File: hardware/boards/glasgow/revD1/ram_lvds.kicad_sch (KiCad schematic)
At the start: 37 parts, among them J11 CLK_EXT, J12 FPGA_TP, J6 LVDS, U11 XccelaOPI, U12 XccelaOPI, U8 LFE5U-25F-8BG256x, Y3 Si5351A-B-GM1, Y4 25M

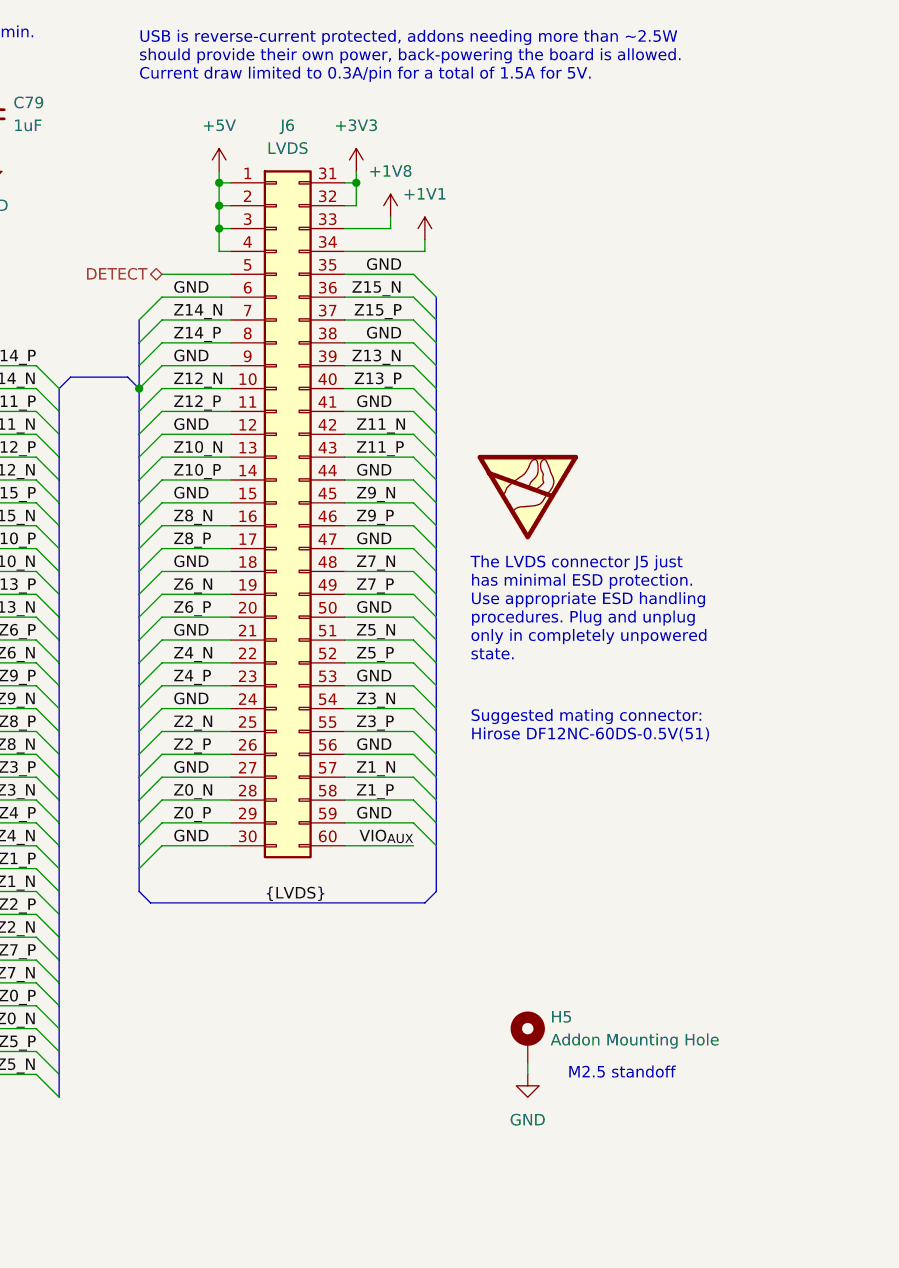
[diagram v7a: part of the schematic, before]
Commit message: update LVDS connector
add more ground test points on the back
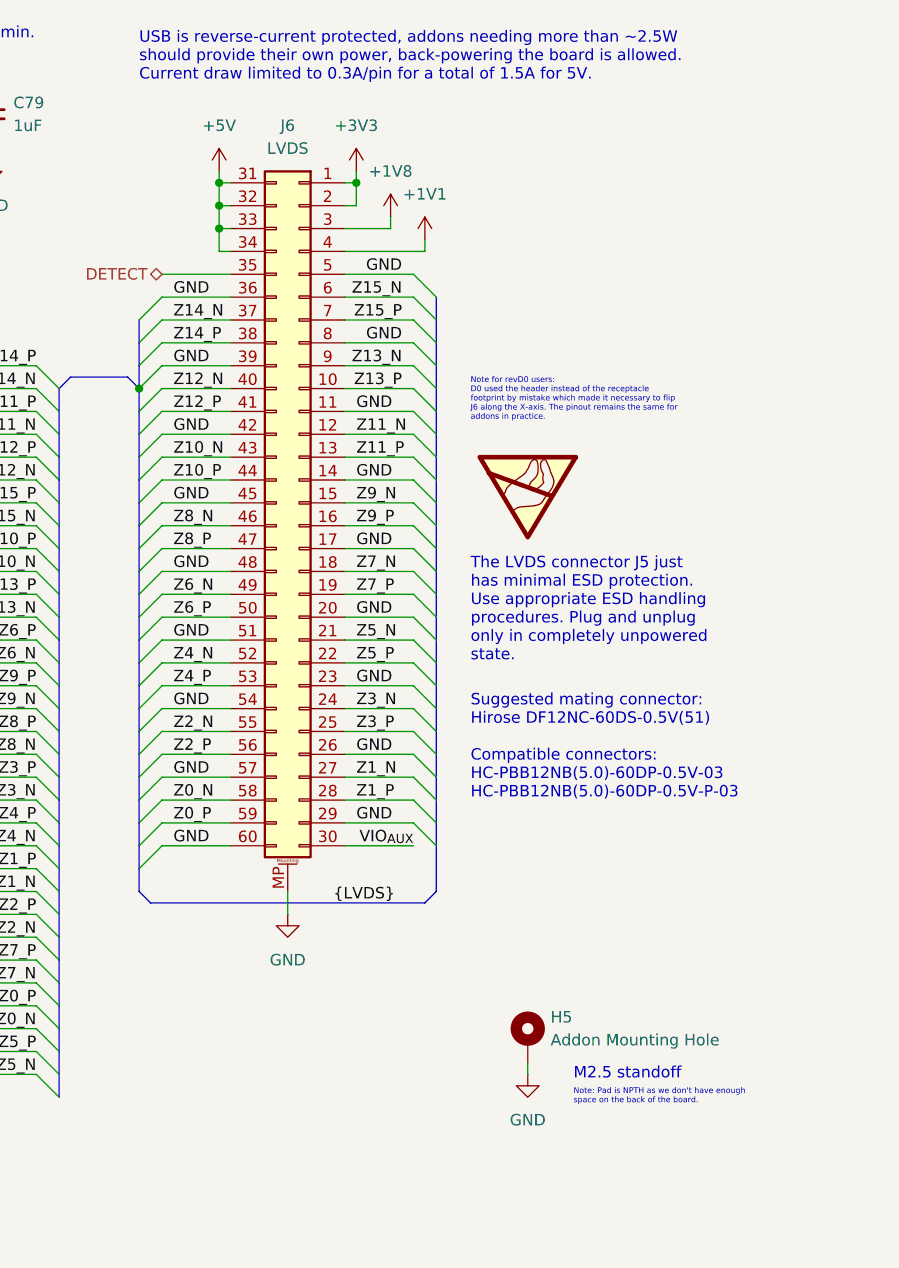
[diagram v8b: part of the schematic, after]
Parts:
- J6: footprint Connector_Hirose:Hirose_DF12_DF12C3.0-60DS-0.5V_2x30_P0.50mm_Vertical -> Automated:Hirose_DF12NB_DF12E3.0-60DP-0.5V_2x30_P0.50mm_Vertical; symbol Connector_Generic:Conn_02x30_Top_Bottom -> Connector_Generic_MountingPin:Conn_02x30_Top_Bottom_MountingPin
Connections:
- net +1V1: now also J6.4 (Pin_4); no longer J6.34 (Pin_34)
- net +1V8: now also J6.3 (Pin_3); no longer J6.33 (Pin_33)
- net +3V3: now also J6.1 (Pin_1), J6.2 (Pin_2); no longer J6.31 (Pin_31), J6.32 (Pin_32)
- net +5V: now also J6.31 (Pin_31), J6.32 (Pin_32), J6.33 (Pin_33), J6.34 (Pin_34); no longer J6.1 (Pin_1), J6.2 (Pin_2), J6.3 (Pin_3), J6.4 (Pin_4)
- net DETECT: now also J6.35 (Pin_35); no longer J6.5 (Pin_5)
- net GND: now also J6.11 (Pin_11), J6.14 (Pin_14), J6.17 (Pin_17), J6.20 (Pin_20), J6.23 (Pin_23), J6.26 (Pin_26), J6.29 (Pin_29), J6.36 (Pin_36), J6.39 (Pin_39), J6.42 (Pin_42), J6.45 (Pin_45), J6.48 (Pin_48), J6.5 (Pin_5), J6.51 (Pin_51), J6.54 (Pin_54), J6.57 (Pin_57), J6.60 (Pin_60), J6.8 (Pin_8), J6.MP (MountPin); no longer J6.12 (Pin_12), J6.15 (Pin_15), J6.18 (Pin_18), J6.21 (Pin_21), J6.24 (Pin_24), J6.27 (Pin_27), J6.30 (Pin_30), J6.35 (Pin_35), J6.38 (Pin_38), J6.41 (Pin_41), J6.44 (Pin_44), J6.47 (Pin_47), J6.50 (Pin_50), J6.53 (Pin_53), J6.56 (Pin_56), J6.59 (Pin_59), J6.6 (Pin_6), J6.9 (Pin_9)
- net VIO_{AUX}: now also J6.30 (Pin_30); no longer J6.60 (Pin_60)
- net Z0_N: now also J6.58 (Pin_58); no longer J6.28 (Pin_28)
- net Z0_P: now also J6.59 (Pin_59); no longer J6.29 (Pin_29)
- net Z10_N: now also J6.43 (Pin_43); no longer J6.13 (Pin_13)
- net Z10_P: now also J6.44 (Pin_44); no longer J6.14 (Pin_14)
- net Z11_N: now also J6.12 (Pin_12); no longer J6.42 (Pin_42)
- net Z11_P: now also J6.13 (Pin_13); no longer J6.43 (Pin_43)
- net Z12_N: now also J6.40 (Pin_40); no longer J6.10 (Pin_10)
- net Z12_P: now also J6.41 (Pin_41); no longer J6.11 (Pin_11)
- net Z13_N: now also J6.9 (Pin_9); no longer J6.39 (Pin_39)
- net Z13_P: now also J6.10 (Pin_10); no longer J6.40 (Pin_40)
- net Z14_N: now also J6.37 (Pin_37); no longer J6.7 (Pin_7)
- net Z14_P: now also J6.38 (Pin_38); no longer J6.8 (Pin_8)
- net Z15_N: now also J6.6 (Pin_6); no longer J6.36 (Pin_36)
- net Z15_P: now also J6.7 (Pin_7); no longer J6.37 (Pin_37)
- net Z1_N: now also J6.27 (Pin_27); no longer J6.57 (Pin_57)
- net Z1_P: now also J6.28 (Pin_28); no longer J6.58 (Pin_58)
- net Z2_N: now also J6.55 (Pin_55); no longer J6.25 (Pin_25)
- net Z2_P: now also J6.56 (Pin_56); no longer J6.26 (Pin_26)
- net Z3_N: now also J6.24 (Pin_24); no longer J6.54 (Pin_54)
- net Z3_P: now also J6.25 (Pin_25); no longer J6.55 (Pin_55)
- net Z4_N: now also J6.52 (Pin_52); no longer J6.22 (Pin_22)
- net Z4_P: now also J6.53 (Pin_53); no longer J6.23 (Pin_23)
- net Z5_N: now also J6.21 (Pin_21); no longer J6.51 (Pin_51)
- net Z5_P: now also J6.22 (Pin_22); no longer J6.52 (Pin_52)
- net Z6_N: now also J6.49 (Pin_49); no longer J6.19 (Pin_19)
- net Z6_P: now also J6.50 (Pin_50); no longer J6.20 (Pin_20)
- net Z7_N: now also J6.18 (Pin_18); no longer J6.48 (Pin_48)
- net Z7_P: now also J6.19 (Pin_19); no longer J6.49 (Pin_49)
- net Z8_N: now also J6.46 (Pin_46); no longer J6.16 (Pin_16)
- net Z8_P: now also J6.47 (Pin_47); no longer J6.17 (Pin_17)
- net Z9_N: now also J6.15 (Pin_15); no longer J6.45 (Pin_45)
- net Z9_P: now also J6.16 (Pin_16); no longer J6.46 (Pin_46)
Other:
- note added: "Note for revD0 users: D0 used the header instead of the receptacle footprint by mistake which made it necessary to flip J6 along the X-axis. The pinout remains the same for addons in practice."
- note added: "Note: Pad is NPTH as we don't have enough space on the back of the board."
- note added: "Suggested mating connector: Hirose DF12NC-60DS-0.5V(51) Compatible connectors: HC-PBB12NB(5.0)-60DP-0.5V-03 HC-PBB12NB(5.0)-60DP-0.5V-P-03"
- note removed: "Suggested mating connector: Hirose DF12NC-60DS-0.5V(51)"
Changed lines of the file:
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@@
 	(title_block
 		(title "FPGA - RAM and LVDS")
-		(date "2026-09-22")
+		(date "2026-09-23")
 		(rev "D1")
 		(company "ln / Fully Automated")
 		(comment 1 "Glasgow Debug Tool")
 	)
+	(text "Note: Pad is NPTH as we don't have enough\nspace on the back of the board."
+		(exclude_from_sim no)
+		(at 256.54 144.78 0)
+		(effects
+			(font
+				(size 0.635 0.635)
+				(color 204 102 0 1)
+			)
+			(justify left)
+		)
+	)
 	(text "VCC_IO3"
 		(exclude_from_sim no)
@@
 		)
 	)
+	(text "Note for revD0 users:\nD0 used the header instead of the receptacle\nfootprint by mistake which made it necessary to flip\nJ6 along the X-axis. The pinout remains the same for\naddons in practice."
+		(exclude_from_sim no)
+		(at 245.11 67.31 0)
+		(effects
+			(font
+				(size 0.635 0.635)
+				(color 204 102 0 1)
+			)
+			(justify left)
+		)
+	)
 	(text "USB is reverse-current protected, addons needing more than ~2.5W\nshould provide their own power, back-powering the board is allowed.\nCurrent draw limited to 0.3A/pin for a total of 1.5A for 5V."
 		(exclude_from_sim no)
@@
 		)
 	)
+	(text "Suggested mating connector:\nHirose DF12NC-60DS-0.5V(51)\n\nCompatible connectors:\nHC-PBB12NB(5.0)-60DP-0.5V-03\nHC-PBB12NB(5.0)-60DP-0.5V-P-03"
+		(exclude_from_sim no)
+		(at 245.11 111.76 0)
+		(effects
+			(font
+				(size 1.27 1.27)
+			)
+			(justify left bottom)
+		)
+	)
 	(text "M2.5 standoff"
 		(exclude_from_sim no)
-		(at 255.905 142.24 0)
+		(at 256.54 142.24 0)
 		(effects
 			(font
@@
 		)
 	)
-	(text "Suggested mating connector:\nHirose DF12NC-60DS-0.5V(51)"
-		(exclude_from_sim no)
-		(at 245.11 105.41 0)
-		(effects
-			(font
-				(size 1.27 1.27)
-			)
-			(justify left bottom)
-		)
-	)
 	(text "RAM ~{RESET} line left floating,\nhas a weak internal pull-up.\n\nCompatible with:\nAPS51208N-OBR-BD\nAPS512XXN-OB9-BG\nAPS512XXN-OBR-BG"
 		(exclude_from_sim no)
@@
 	(wire
 		(pts
-			(xy 218.44 114.3) (xy 210.82 114.3)
-		)
-		(stroke
-			(width 0)
-			(type default)
-		)
-	)
-	(wire
-		(pts
 			(xy 161.29 166.37) (xy 171.45 166.37)
 		)
@@
 	(wire
 		(pts
-			(xy 218.44 68.58) (xy 210.82 68.58)
+			(xy 111.76 163.83) (xy 113.03 163.83)
 		)
 		(stroke
@@
 	(wire
 		(pts
-			(xy 111.76 163.83) (xy 113.03 163.83)
+			(xy 106.68 21.59) (xy 106.68 22.86)
 		)
 		(stroke
@@
 	(wire
 		(pts
-			(xy 106.68 21.59) (xy 106.68 22.86)
+			(xy 59.69 71.12) (xy 67.31 71.12)
 		)
 		(stroke
@@
 	(wire
 		(pts
-			(xy 59.69 71.12) (xy 67.31 71.12)
+			(xy 210.82 68.58) (xy 218.44 68.58)
 		)
 		(stroke
@@
 	(wire
 		(pts
-			(xy 218.44 76.2) (xy 210.82 76.2)
-		)
-		(stroke
-			(width 0)
-			(type default)
-		)
-	)
-	(wire
-		(pts
 			(xy 59.69 127) (xy 66.04 127)
 		)
@@
 		)
 	)
+	(wire
+		(pts
+			(xy 210.82 76.2) (xy 218.44 76.2)
+		)
+		(stroke
+			(width 0)
+			(type default)
+		)
+	)
 	(bus
 		(pts
@@
 	(wire
 		(pts
-			(xy 218.44 99.06) (xy 210.82 99.06)
-		)
-		(stroke
-			(width 0)
-			(type default)
-		)
-	)
-	(wire
-		(pts
 			(xy 77.47 124.46) (xy 77.47 123.19)
 		)
@@
 	(wire
 		(pts
-			(xy 218.44 106.68) (xy 210.82 106.68)
-		)
-		(stroke
-			(width 0)
-			(type default)
-		)
-	)
-	(wire
-		(pts
 			(xy 171.45 39.37) (xy 181.61 39.37)
 		)
@@
 		)
 	)
+	(wire
+		(pts
+			(xy 210.82 114.3) (xy 218.44 114.3)
+		)
+		(stroke
+			(width 0)
+			(type default)
+		)
+	)
 	(bus
 		(pts
@@
 	(wire
 		(pts
+			(xy 210.82 91.44) (xy 218.44 91.44)
+		)
+		(stroke
+			(width 0)
+			(type default)
+		)
+	)
+	(wire
+		(pts
 			(xy 77.47 81.28) (xy 77.47 80.01)
 		)
@@
 	(wire
 		(pts
-			(xy 218.44 83.82) (xy 210.82 83.82)
-		)
-		(stroke
-			(width 0)
-			(type default)
-		)
-	)
-	(wire
-		(pts
 			(xy 231.14 66.04) (xy 238.76 66.04)
 		)
@@
 	(wire
 		(pts
-			(xy 218.44 91.44) (xy 210.82 91.44)
-		)
-		(stroke
-			(width 0)
-			(type default)
-		)
-	)
-	(wire
-		(pts
 			(xy 165.1 30.48) (xy 171.45 30.48)
 		)
@@
 	(wire
 		(pts
+			(xy 210.82 99.06) (xy 218.44 99.06)
+		)
+		(stroke
+			(width 0)
+			(type default)
+		)
+	)
+	(wire
+		(pts
 			(xy 190.5 129.54) (xy 196.85 129.54)
 		)
@@
 	(wire
 		(pts
+			(xy 210.82 106.68) (xy 218.44 106.68)
+		)
+		(stroke
+			(width 0)
+			(type default)
+		)
+	)
+	(wire
+		(pts
 			(xy 210.82 109.22) (xy 218.44 109.22)
 		)
@@
 		)
 	)
+	(wire
+		(pts
+			(xy 210.82 83.82) (xy 218.44 83.82)
+		)
+		(stroke
+			(width 0)
+			(type default)
+		)
+	)
 	(bus
 		(pts
@@
 	(wire
 		(pts
+			(xy 210.82 60.96) (xy 218.44 60.96)
+		)
+		(stroke
+			(width 0)
+			(type default)
+		)
+	)
+	(wire
+		(pts
 			(xy 59.69 116.84) (xy 66.04 116.84)
 		)
@@
 	(wire
 		(pts
-			(xy 218.44 60.96) (xy 210.82 60.96)
+			(xy 224.79 121.92) (xy 224.79 124.46)
 		)
 		(stroke
@@
 	)
 	(label "{LVDS}"
-		(at 222.25 123.19 0)
+		(at 229.87 123.19 0)
 		(effects
 			(font
@@
 	)
 	(symbol
+		(lib_id "power:GND")
+		(at 224.79 124.46 0)
+		(unit 1)
+		(body_style 1)
+		(exclude_from_sim no)
+		(in_bom yes)
+		(on_board yes)
+		(in_pos_files yes)
+		(dnp no)
+		(fields_autoplaced yes)
+		(property "Reference" "#PWR0428"
+			(at 224.79 130.81 0)
+			(hide yes)
+			(show_name no)
+			(do_not_autoplace no)
+			(effects
+				(font
+					(size 1.27 1.27)
+				)
+			)
+		)
+		(property "Value" "GND"
+			(at 224.79 129.54 0)
+			(show_name no)
+			(do_not_autoplace no)
+			(effects
+				(font
+					(size 1.27 1.27)
+				)
+			)
+		)
+		(property "Footprint" ""
+			(at 224.79 124.46 0)
+			(hide yes)
+			(show_name no)
+			(do_not_autoplace no)
+			(effects
+				(font
+					(size 1.27 1.27)
+				)
+			)
+		)
+		(property "Datasheet" ""
+			(at 224.79 124.46 0)
+			(hide yes)
+			(show_name no)
+			(do_not_autoplace no)
+			(effects
+				(font
+					(size 1.27 1.27)
+				)
+			)
+		)
+		(property "Description" "Power symbol creates a global label with name \"GND\" , ground"
+			(at 224.79 124.46 0)
+			(hide yes)
+			(show_name no)
+			(do_not_autoplace no)
+			(effects
+				(font
+					(size 1.27 1.27)
+				)
+			)
+		)
+		(pin "1"
+		)
+		(instances
+			(project "glasgow"
+				(path "/87a94d88-8a34-4311-9666-80951c15f2c0/6df960f8-fdad-40ff-9ddd-1dfb6db1717e/eeead648-5da8-4d82-bed0-cbbdd6dbf004"
+					(reference "#PWR0428")
+					(unit 1)
+				)
+			)
+		)
+	)
+	(symbol
 		(lib_id "power:+5V")
 		(at 217.17 41.91 0)
@@
 	)
 	(symbol
-		(lib_id "Connector_Generic:Conn_02x30_Top_Bottom")
-		(at 223.52 78.74 0)
+		(lib_id "Connector_Generic_MountingPin:Conn_02x30_Top_Bottom_MountingPin")
+		(at 226.06 78.74 0)
+		(mirror y)
 		(unit 1)
 		(body_style 1)
@@
 			)
 		)
-		(property "Footprint" "Connector_Hirose:Hirose_DF12_DF12C3.0-60DS-0.5V_2x30_P0.50mm_Vertical"
-			(at 223.52 78.74 0)
+		(property "Footprint" "Automated:Hirose_DF12NB_DF12E3.0-60DP-0.5V_2x30_P0.50mm_Vertical"
+			(at 226.06 78.74 0)
 			(hide yes)
 			(show_name no)
@@
 		)
 		(property "Datasheet" "https://www.hirose.com/en/product/document?clcode=&productname=&series=DF12N&documenttype=Catalog&lang=en&documentid=ed_DF12N_20200819"
-			(at 223.52 78.74 0)
+			(at 226.06 78.74 0)
 			(hide yes)
 			(show_name no)
@@
 			)
 		)
-		(property "Description" "Generic connector, double row, 02x30, top/bottom pin numbering scheme (row 1: 1...pins_per_row, row2: pins_per_row+1 ... num_pins), script generated (kicad-library-utils/schlib/autogen/connector/)"
-			(at 223.52 78.74 0)
+		(property "Description" "Generic connectable mounting pin connector, double row, 02x30, top/bottom pin numbering scheme (row 1: 1...pins_per_row, row2: pins_per_row+1 ... num_pins), script generated (kicad-library-utils/schlib/autogen/connector/)"
+			(at 226.06 78.74 0)
 			(hide yes)
 			(show_name no)
@@
 		)
 		(property "LCSC" "C3645041"
-			(at 223.52 78.74 0)
+			(at 226.06 78.74 0)
 			(hide yes)
 			(show_name no)
@@
 		)
 		(property "MPN" "DF12NC(5.0)-60DP-0.5V(51)"
-			(at 223.52 78.74 0)
+			(at 226.06 78.74 0)
 			(hide yes)
 			(show_name no)
@@
 		)
 		(property "KLC_S4.1" ""
-			(at 223.52 78.74 0)
+			(at 226.06 78.74 0)
 			(hide yes)
 			(show_name no)
@@
 		(pin "20"
 		)
+		(pin "MP"
+		)
 		(instances
 			(project "glasgow"
@@
 			)
 		)
-		(property "Datasheet" ""
+		(property "Datasheet" "https://www.we-online.com/components/products/datasheet/9774050151R.pdf"
 			(at 251.46 138.43 0)
 			(hide yes)
